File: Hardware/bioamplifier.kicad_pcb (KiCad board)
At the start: 4 copper layers, 54.5 x 54.7 mm, 65 parts, among them J1 Conn_01x40_Pin, J2 Conn_01x26_Pin, U1 ADS1299IPAG, U10 TPD4E1B06DCKR, U2 TPD4E1B06DCKR, U3 TPD4E1B06DCKR, U4 TPD4E1B06DCKR, U5 TPD4E1B06DCKR, U7 TPS73133DBV, U8 TPS73201DCQ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

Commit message: schematics redone, TODO: Pcb component placement
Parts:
- added C42: 2.2 nF, Capacitor_SMD:C_0603_1608Metric, F.Cu at (133.3, 94.6)
- added C43: 2.2 nF, Capacitor_SMD:C_0603_1608Metric, F.Cu at (133.3, 97.1)
- added C44: 10 nF, Capacitor_SMD:C_0603_1608Metric, F.Cu at (133.3, 99.7)
- added C45: 10 u, Capacitor_SMD:C_0603_1608Metric, F.Cu at (133.3, 102.2)
- added C46: 10 u, Capacitor_SMD:C_0603_1608Metric, F.Cu at (133.3, 104.7)
- added IC1: MCP1754ST-3302E_DB, mcp1754:SOT230P700X180-4N, F.Cu at (140.1, 106.8)
- added J3: Conn_01x08_Socket, Connector_PinHeader_2.54mm:PinHeader_1x08_P2.54mm_Vertical, F.Cu at (104.2, 68.0)
- added R10: 50, Resistor_SMD:R_0402_1005Metric, F.Cu at (115.2, 79.0)
- added R11: 50, Resistor_SMD:R_0402_1005Metric, F.Cu at (115.2, 76.3)
- added R12: 50, Resistor_SMD:R_0402_1005Metric, F.Cu at (115.2, 74.3)
- added R13: 50, Resistor_SMD:R_0402_1005Metric, F.Cu at (115.2, 71.5)
- added R14: 50, Resistor_SMD:R_0402_1005Metric, F.Cu at (115.2, 68.5)
- added R15: 50, Resistor_SMD:R_0402_1005Metric, F.Cu at (115.5, 66.0)
- added R3: 50, Resistor_SMD:R_0402_1005Metric, F.Cu at (100.5, 68.0)
- added R4: 50, Resistor_SMD:R_0402_1005Metric, F.Cu at (100.5, 70.5)
- added R5: 50, Resistor_SMD:R_0402_1005Metric, F.Cu at (100.5, 73.0)
- added R6: 50, Resistor_SMD:R_0402_1005Metric, F.Cu at (100.5, 75.6)
- added R7: 50, Resistor_SMD:R_0402_1005Metric, F.Cu at (100.5, 77.7)
- added R8: 50, Resistor_SMD:R_0402_1005Metric, F.Cu at (100.5, 80.7)
- added R9: 50, Resistor_SMD:R_0402_1005Metric, F.Cu at (115.2, 81.5)
- added U11: LM2665M6, Package_TO_SOT_SMD:SOT-23-6, F.Cu at (137.9, 100.4)
- added U12: TLV77333PDQNR, tlv77333:X2SON_DQN4_TEX, F.Cu at (142.0, 94.7)
- added U6: TPS73133DBV, Package_TO_SOT_SMD:SOT-23-5, F.Cu at (137.9, 95.8)
- C25, C40: value 1 nF -> 1 nF
- J1: value Conn_01x40_Pin -> Conn_01x08_Socket; footprint Connector_PinHeader_2.54mm:PinHeader_2x20_P2.54mm_Vertical -> Connector_PinHeader_2.54mm:PinHeader_1x08_P2.54mm_Vertical
- U7: value TPS73133DBV -> TPS72325DBV
- moved J1 33.3 mm to (119.2, 83.9)
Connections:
- C1 pad 1: /AVDD -> AVDD
- C21 pad 1: /AVDD -> AVDD
- C22 pad 1: /AVDD -> AVDD
- C23 pad 1: /AVDD -> AVDD
- C24 pad 2: /AVDD -> AVDD
- C25 pad 1: Net-(U8-NR/FB) -> /Volt_regulators_inverters/5V_UNREG
- C27 pad 1: /3.3V_UNREG -> 3.3V_UNREG
- C29 pad 1: Net-(U7-NR) -> Net-(U6-NR)
- C40 pad 1: /5V_UNREG -> Net-(U8-NR/FB)
- C41 pad 1: /DVDD -> Net-(U6-NR)
- J1 pad 1: /3.3V_UNREG -> GNDD
- J1 pad 2: unconnected-(J1-Pin_2-Pad2) -> Net-(J1-Pin_2)
- J1 pad 3: unconnected-(J1-Pin_3-Pad3) -> Net-(J1-Pin_3)
- J1 pad 4: /5V_UNREG -> Net-(J1-Pin_4)
- J1 pad 5: unconnected-(J1-Pin_5-Pad5) -> Net-(J1-Pin_5)
- J1 pad 6: unconnected-(J1-Pin_6-Pad6) -> Net-(J1-Pin_6)
- J1 pad 7: unconnected-(J1-Pin_7-Pad7) -> Net-(J1-Pin_7)
- J1 pad 8: unconnected-(J1-Pin_8-Pad8) -> Net-(J1-Pin_8)
- U1 pad 19: /AVDD -> AVDD
- U1 pad 21: /AVDD -> AVDD
- U1 pad 22: /AVDD -> AVDD
- U1 pad 54: /AVDD -> AVDD
- U1 pad 56: /AVDD -> AVDD
- U1 pad 59: /AVDD -> AVDD
- U7 pad 1: /3.3V_UNREG -> GNDA
- U7 pad 2: GNDA -> -2.5V_UNREG
- U7 pad 3: /3.3V_UNREG -> DVDD
- U7 pad 5: /DVDD -> AVSS
- U8 pad 1: /5V_UNREG -> /Volt_regulators_inverters/5V_UNREG
- U8 pad 2: /AVDD -> /Volt_regulators_inverters/AVDD
- U8 pad 5: /5V_UNREG -> /Volt_regulators_inverters/5V_UNREG
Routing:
- net (no net): track 0.00 -> 107.3 mm, vias 0 -> 2
- net /AVDD: track 59.5 -> 0.00 mm, vias 2 -> 0
- net /START_CONV: track 30.8 -> 0.00 mm
- net /3.3V_UNREG: track 27.4 -> 0.00 mm
- net /GPIO3: track 25.3 -> 0.00 mm, vias 1 -> 0
- net /GPIO4: track 24.7 -> 0.00 mm, vias 1 -> 0
- net /GPIO2: track 22.1 -> 0.00 mm, vias 2 -> 0
- net /DRDY: track 21.9 -> 0.00 mm
- net /PWDN: track 21.6 -> 0.00 mm
- net /SCLK: track 21.1 -> 0.00 mm
- net /RESET: track 20.7 -> 0.00 mm
- net /5V_UNREG: track 20.4 -> 0.00 mm
- net /DOUT: track 20.1 -> 0.00 mm, vias 1 -> 0
- net /CHIP_SEL: track 17.8 -> 0.00 mm
- net /DIN: track 19.5 -> 4.30 mm
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
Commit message: changes to pcb and schematics
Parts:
- removed R15: 50, Resistor_SMD:R_0402_1005Metric
- J1: value Conn_01x08_Socket -> Conn_01x07_Socket; footprint Connector_PinHeader_2.54mm:PinHeader_1x08_P2.54mm_Vertical -> Connector_PinHeader_2.54mm:PinHeader_1x07_P2.54mm_Vertical
- moved U7 53.6 mm to (129.4, 76.0)
- moved C27 46.5 mm to (114.0, 74.3), turned to -90 degrees
- moved C29 43.0 mm to (121.0, 78.8)
- moved R14 39.9 mm to (94.0, 102.2), turned to -90 degrees
- moved C41 37.9 mm to (118.5, 80.8), turned to 180 degrees
- moved R13 36.1 mm to (96.2, 102.2), turned to -90 degrees
- moved R12 32.4 mm to (98.9, 102.2), turned to -90 degrees
- moved R11 29.4 mm to (101.6, 102.2), turned to -90 degrees
- moved U6 29.3 mm to (117.8, 74.5)
- moved R10 25.7 mm to (104.2, 102.2), turned to -90 degrees
- moved J1 24.1 mm to (109.2, 105.8), turned to -90 degrees
- moved U8 22.6 mm to (114.4, 88.8), turned to -90 degrees
- moved R9 22.5 mm to (106.6, 102.2), turned to -90 degrees
- moved C40 22.2 mm to (107.9, 89.3)
- moved C42 21.9 mm to (125.8, 74.0), turned to 90 degrees
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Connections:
- C25 pad 1: /Volt_regulators_inverters/5V_UNREG -> 5V_UNREG
- J3 pad 7: 3.3V_UNREG -> 5V_UNREG
- J3 pad 8: 5V_UNREG -> 3.3V_UNREG
- R10 pad 1: /GPIO3 -> /CHIP_SEL
- R11 pad 1: /GPIO2 -> /START_CONV
- R12 pad 1: /GPIO1 -> /RESET
- R13 pad 1: /RESET -> /PWDN
- R14 pad 1: /PWDN -> /DIN
- R3 pad 1: /SCLK -> /DRDY
- R4 pad 1: /START_CONV -> /GPIO4
- R5 pad 1: /DRDY -> /GPIO3
- R6 pad 1: /CHIP_SEL -> /GPIO2
- R7 pad 1: /DIN -> /DOUT
- R8 pad 1: /DOUT -> /GPIO1
- R9 pad 1: /GPIO4 -> /SCLK
- U8 pad 1: /Volt_regulators_inverters/5V_UNREG -> 5V_UNREG
- U8 pad 2: /Volt_regulators_inverters/AVDD -> AVDD
- U8 pad 5: /Volt_regulators_inverters/5V_UNREG -> 5V_UNREG
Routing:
- net (no net): track 107.3 -> 0.00 mm, vias 2 -> 0
- net AVDD: track 0.00 -> 78.1 mm, vias 0 -> 4
- net /SCLK: track 0.00 -> 27.2 mm
- net 5V_UNREG: track 0.00 -> 26.7 mm
- net /CHIP_SEL: track 0.00 -> 24.6 mm
- net GNDA: track 75.7 -> 53.0 mm, vias 7 -> 4
- net /DOUT: track 0.00 -> 21.9 mm
- net /START_CONV: track 0.00 -> 21.8 mm
- net /GPIO2: track 0.00 -> 19.6 mm
- net Net-(D1-A): track 0.00 -> 19.2 mm
- net /RESET: track 0.00 -> 18.7 mm
- net /GPIO3: track 0.00 -> 16.7 mm
- net /PWDN: track 0.00 -> 16.4 mm
- net /GPIO4: track 0.00 -> 14.0 mm
- net /DRDY: track 0.00 -> 12.0 mm
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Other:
- board size 54.5 x 54.7 mm -> 73.2 x 44.5 mm

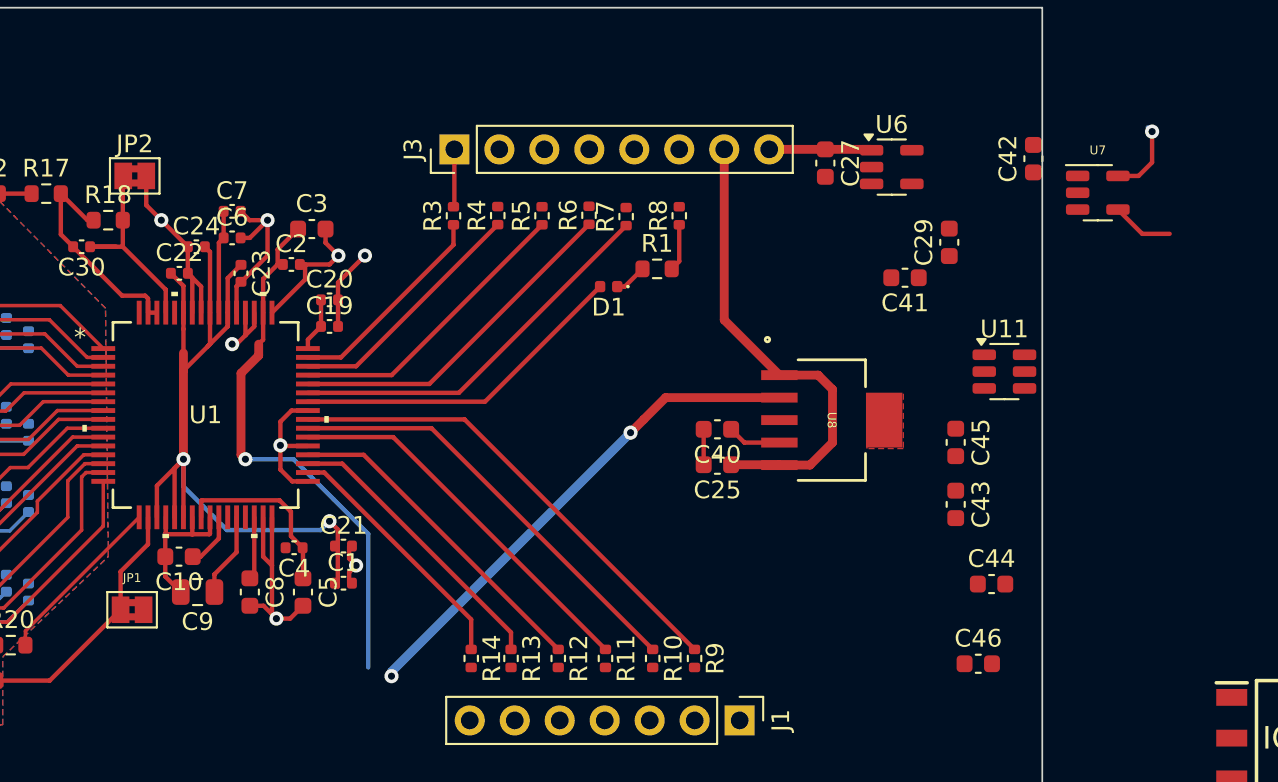
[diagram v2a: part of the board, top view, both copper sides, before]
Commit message: removed 5V LDO Regulator
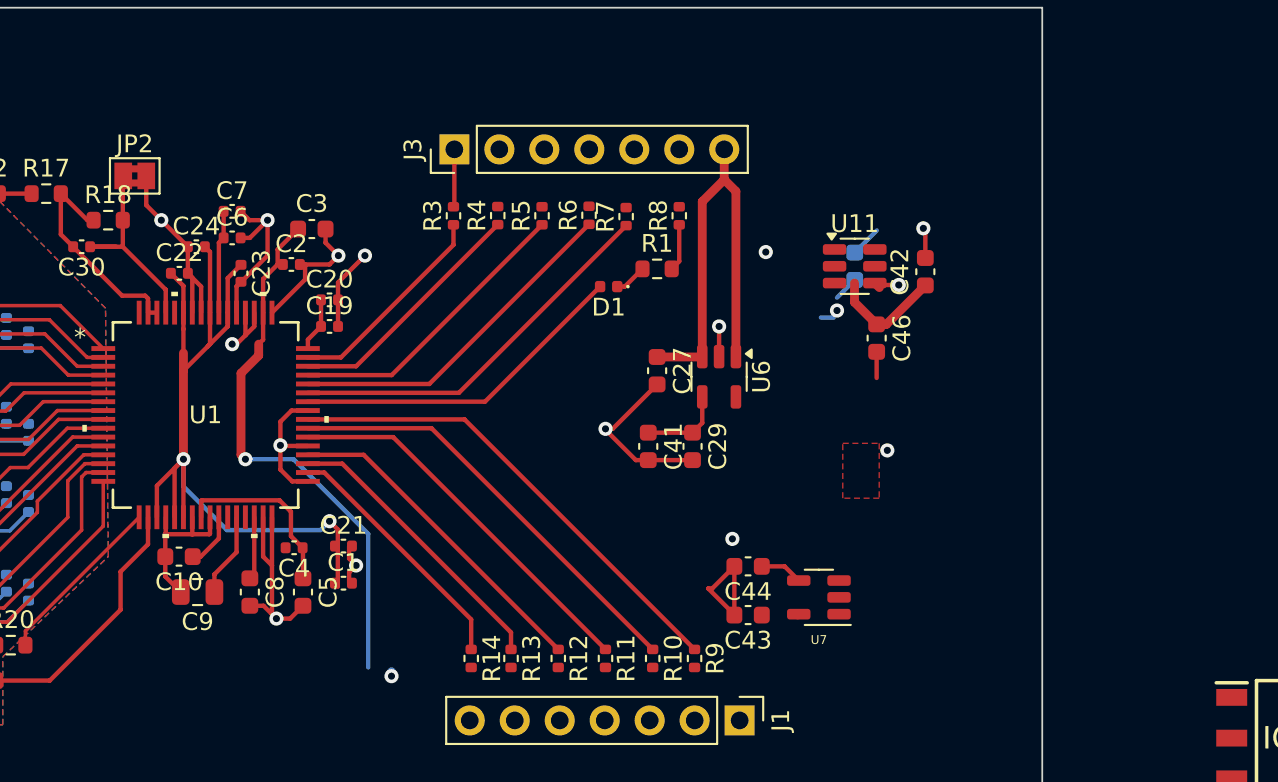
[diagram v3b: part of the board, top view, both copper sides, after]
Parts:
- removed C25, C40: 1 nF, Capacitor_SMD:C_0603_1608Metric
- removed JP1: Jumper_2_Bridged, Jumper:SolderJumper-2_P1.3mm_Bridged2Bar_Pad1.0x1.5mm
- removed U8: TPS73201DCQ, tps732:DCQ6_TEX
- C45: moved to B.Cu
- J3: value Conn_01x08_Socket -> Conn_01x07_Socket; footprint Connector_PinHeader_2.54mm:PinHeader_1x08_P2.54mm_Vertical -> Connector_PinHeader_2.54mm:PinHeader_1x07_P2.54mm_Vertical
- moved U7 27.8 mm to (113.6, 98.8), turned to 180 degrees
- moved C46 19.3 mm to (116.9, 84.2), turned to -90 degrees
- moved C29 18.5 mm to (106.5, 90.3), turned to -90 degrees
- moved C41 17.3 mm to (104.0, 90.3), turned to -90 degrees
- moved U6 15.3 mm to (108.0, 86.3), turned to -90 degrees
- moved C27 15.1 mm to (104.5, 86.0)
- moved C44 13.8 mm to (109.6, 97.0), turned to 180 degrees
- moved C43 13.3 mm to (109.6, 99.8), turned to 180 degrees
- moved C45 11.5 mm to (115.7, 80.1)
- moved U11 10.3 mm to (115.7, 80.1)
- moved C42 8.83 mm to (119.6, 80.4)
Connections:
- C46 pad 1: AVSS -> -2.5V_UNREG
- J3 pad 7: 5V_UNREG -> 3.3V_UNREG
- U11 pad 5: AVSS -> -2.5V_UNREG
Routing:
- net AVDD: track 78.1 -> 49.7 mm, vias 4 -> 3
- net 5V_UNREG: track 26.7 -> 0.00 mm
- net GNDA: track 53.0 -> 72.4 mm, vias 4 -> 10
- net 3.3V_UNREG: track 5.80 -> 25.0 mm
- net -2.5V_UNREG: track 0.00 -> 6.52 mm
- net Net-(U6-NR): track 0.00 -> 4.75 mm
- net AVSS: track 4.33 -> 0.07 mm, vias 1 -> 0
- net Net-(U8-NR/FB): track 3.04 -> 0.00 mm
- net Net-(U11-CAP-): track 0.00 -> 2.33 mm, vias 0 -> 1
- net DVDD: track 0.00 -> 2.27 mm, vias 0 -> 1
- net Net-(U11-CAP+): track 0.00 -> 1.93 mm
- net Net-(U7-NR): track 3.49 -> 2.42 mm

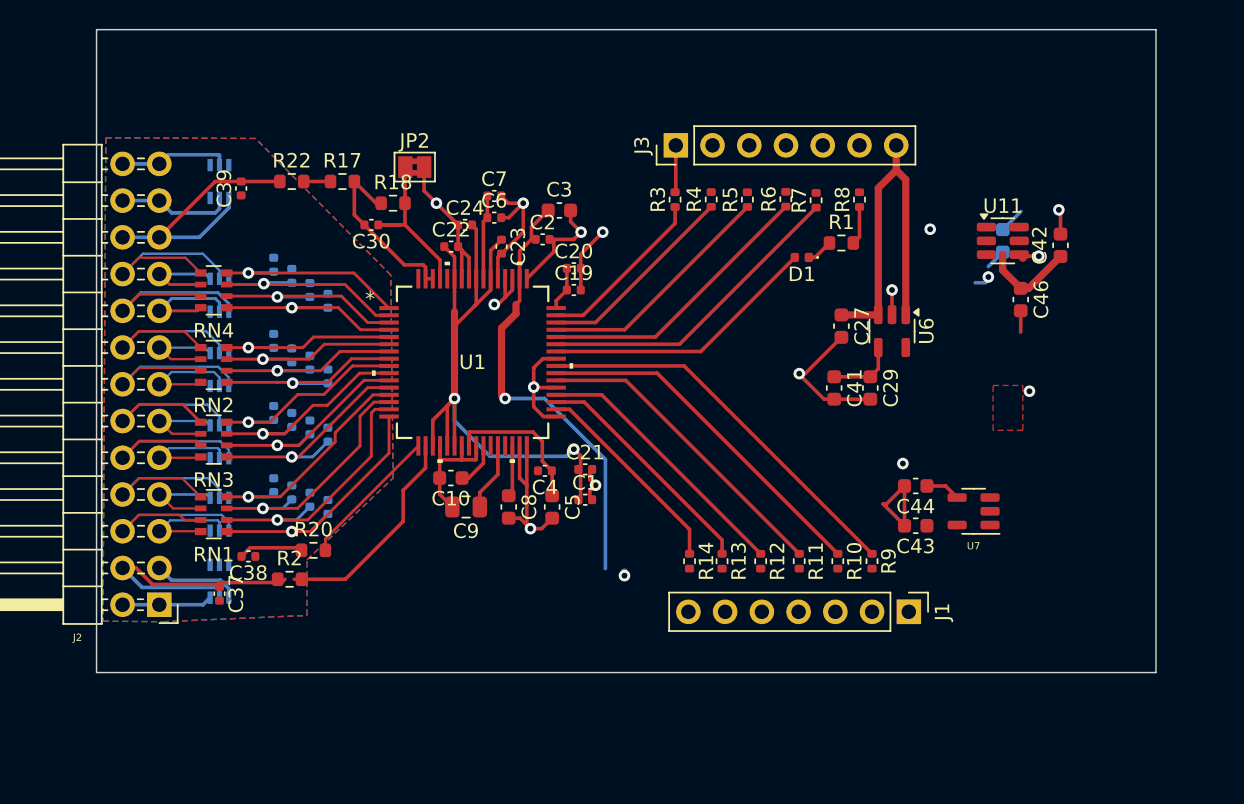
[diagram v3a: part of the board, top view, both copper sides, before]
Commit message: power pin layout change
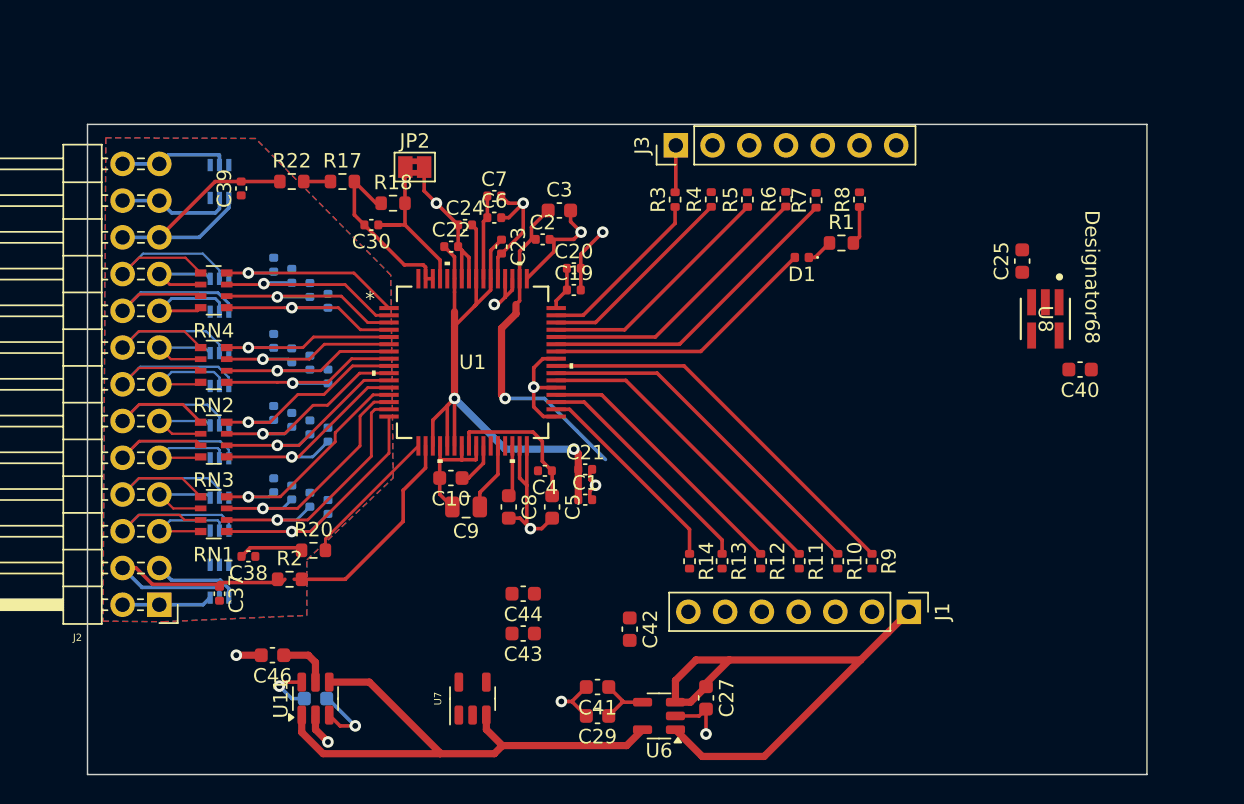
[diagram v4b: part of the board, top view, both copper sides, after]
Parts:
- added C25: 0.1u, Capacitor_SMD:C_0603_1608Metric, F.Cu at (117.0, 81.5)
- added C40: 0.1u, Capacitor_SMD:C_0603_1608Metric, F.Cu at (121.0, 89.0)
- added U8: TLV70310DBVR, tlv702:DBV0005A-IPC_A, F.Cu at (118.6, 85.5)
- moved C46 57.3 mm to (65.2, 108.8), turned to 180 degrees
- moved C45 57.1 mm to (68.1, 111.8), turned to 0 degrees
- moved U11 57.1 mm to (68.1, 111.8), turned to 90 degrees
- moved C42 39.9 mm to (89.9, 107.0), turned to -90 degrees
- moved U7 37.0 mm to (79.0, 111.8), turned to 90 degrees
- moved U6 31.1 mm to (91.9, 113.0), turned to 180 degrees
- moved C29 29.5 mm to (87.6, 113.0), turned to 180 degrees
- moved C43 28.1 mm to (82.5, 107.2)
- moved C44 28.1 mm to (82.5, 104.5)
- moved C27 27.4 mm to (95.1, 111.7)
- moved C41 26.4 mm to (87.6, 111.0), turned to 180 degrees
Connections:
- C1 pad 2: GNDA -> GNDD
- C10 pad 2: GNDA -> AVSS
- C11 pad 1: GNDA -> AVSS
- C12 pad 1: GNDA -> AVSS
- C13 pad 1: GNDA -> AVSS
- C14 pad 1: GNDA -> AVSS
- C15 pad 1: GNDA -> AVSS
- C16 pad 1: GNDA -> AVSS
- C17 pad 1: GNDA -> AVSS
- C18 pad 1: GNDA -> AVSS
- C21 pad 2: GNDA -> AVSS
- C22 pad 2: GNDA -> AVSS
- C23 pad 2: GNDA -> AVSS
- C24 pad 1: GNDA -> AVSS
- C26 pad 1: GNDA -> AVSS
- C27 pad 2: GNDA -> GNDD
- C28 pad 1: GNDA -> AVSS
- C29 pad 2: GNDA -> GNDD
- C31 pad 1: GNDA -> AVSS
- C32 pad 1: GNDA -> AVSS
- C33 pad 1: GNDA -> AVSS
- C34 pad 1: GNDA -> AVSS
- C35 pad 1: GNDA -> AVSS
- C36 pad 1: GNDA -> AVSS
- C37 pad 2: GNDA -> AVSS
- C38 pad 1: GNDA -> AVSS
- C39 pad 1: GNDA -> AVSS
- C4 pad 2: GNDA -> AVSS
- C41 pad 2: GNDA -> GNDD
- C42 pad 2: GNDA -> AVSS
- C43 pad 2: GNDA -> AVSS
- C44 pad 2: GNDA -> AVSS
- C46 pad 2: GNDA -> AVSS
- C5 pad 2: GNDA -> AVSS
- C6 pad 2: GNDA -> AVSS
- C7 pad 2: GNDA -> AVSS
- C8 pad 2: GNDA -> AVSS
- C9 pad 2: GNDA -> AVSS
- J1 pad 1: GNDD -> 3.3V_UNREG
- J2 pad 1: GNDA -> AVSS
- J2 pad 2: GNDA -> AVSS
- J3 pad 7: 3.3V_UNREG -> GNDD
- JP2 pad 2: GNDA -> AVSS
- U1 pad 20: GNDA -> AVSS
- U1 pad 23: GNDA -> GNDD
- U1 pad 25: GNDA -> AVSS
- U1 pad 31: GNDA -> AVSS
- U1 pad 32: GNDA -> AVSS
- U1 pad 53: GNDA -> AVSS
- U1 pad 57: GNDA -> AVSS
- U1 pad 58: GNDA -> AVSS
- U1 pad 60: GNDA -> AVSS
- U10 pad 3: GNDA -> AVSS
- U11 pad 2: GNDA -> AVSS
- U2 pad 3: GNDA -> AVSS
- U3 pad 3: GNDA -> AVSS
- U4 pad 3: GNDA -> AVSS
- U5 pad 3: GNDA -> AVSS
- U6 pad 2: GNDA -> GNDD
- U7 pad 1: GNDA -> AVSS
- U9 pad 3: GNDA -> AVSS
- U9 pad 4: GNDA -> AVSS
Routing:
- net GNDA: track 72.4 -> 0.00 mm, vias 10 -> 0
- net AVSS: track 0.07 -> 43.5 mm, vias 0 -> 6
- net DVDD: track 2.27 -> 38.4 mm, vias 1 -> 0
- net 3.3V_UNREG: track 25.0 -> 41.0 mm
- net (no net): track 0.00 -> 11.4 mm
- net GNDD: track 23.6 -> 31.2 mm, vias 4 -> 6
- net /DVDD: track 30.7 -> 23.1 mm
- net Net-(U11-CAP-): track 2.33 -> 4.87 mm
- net -2.5V_UNREG: track 6.52 -> 4.09 mm
- net Net-(U7-NR): track 2.42 -> 0.00 mm
- net AVDD: track 49.7 -> 47.9 mm, vias 3 -> 2
- net Net-(U11-CAP+): track 1.93 -> 3.75 mm, vias 0 -> 1
- net Net-(U6-NR): track 4.75 -> 4.17 mm
- added copper zone on In2.Cu, net /DVDD
- added copper zone on B.Cu, net AVSS
- added copper zone on F.Cu, net AVSS
- added copper zone on In1.Cu, net AVSS
- added copper zone on In1.Cu, net GNDD
- removed copper zone on B.Cu, net GNDA
- removed copper zone on F.Cu, net GNDA
- removed copper zone on In1.Cu, net GNDA
- removed copper zone on In2.Cu, net GNDD
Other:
- board size 73.2 x 44.5 mm -> 73.2 x 45 mm
